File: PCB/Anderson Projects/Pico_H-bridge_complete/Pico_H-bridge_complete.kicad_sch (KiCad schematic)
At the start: 40 parts, among them J1 Screw_Terminal_01x10, J2 Motor Connector, SW1 SW_DIP_x01, U1 Pico, U2 ILD217T, U3 ILD217T, U4 ILD217T, U5 OPA4197

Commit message: Anderson Schematic with opto-couples prior to change to zener diodes
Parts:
- added C20: 0.1uF, Capacitor_SMD:C_0805_2012Metric, symbol Device:C
- added C21: 1uF, Capacitor_SMD:C_0805_2012Metric, symbol Device:C
- D3: value 3.6V -> 3.3v
- R10, R4, R6, R8: value 4.7k -> 10k
- R21, R23: value 4.7k -> 1kΩ
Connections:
- net +3.3V: now also U1.35 (ADC_VREF), C20.1, C21.1
- net GND: now also U1.33 (AGND), C20.2, C21.2
- no-connect marks 20 -> 18
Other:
- moved on the sheet: D3, R24, R25, RV1

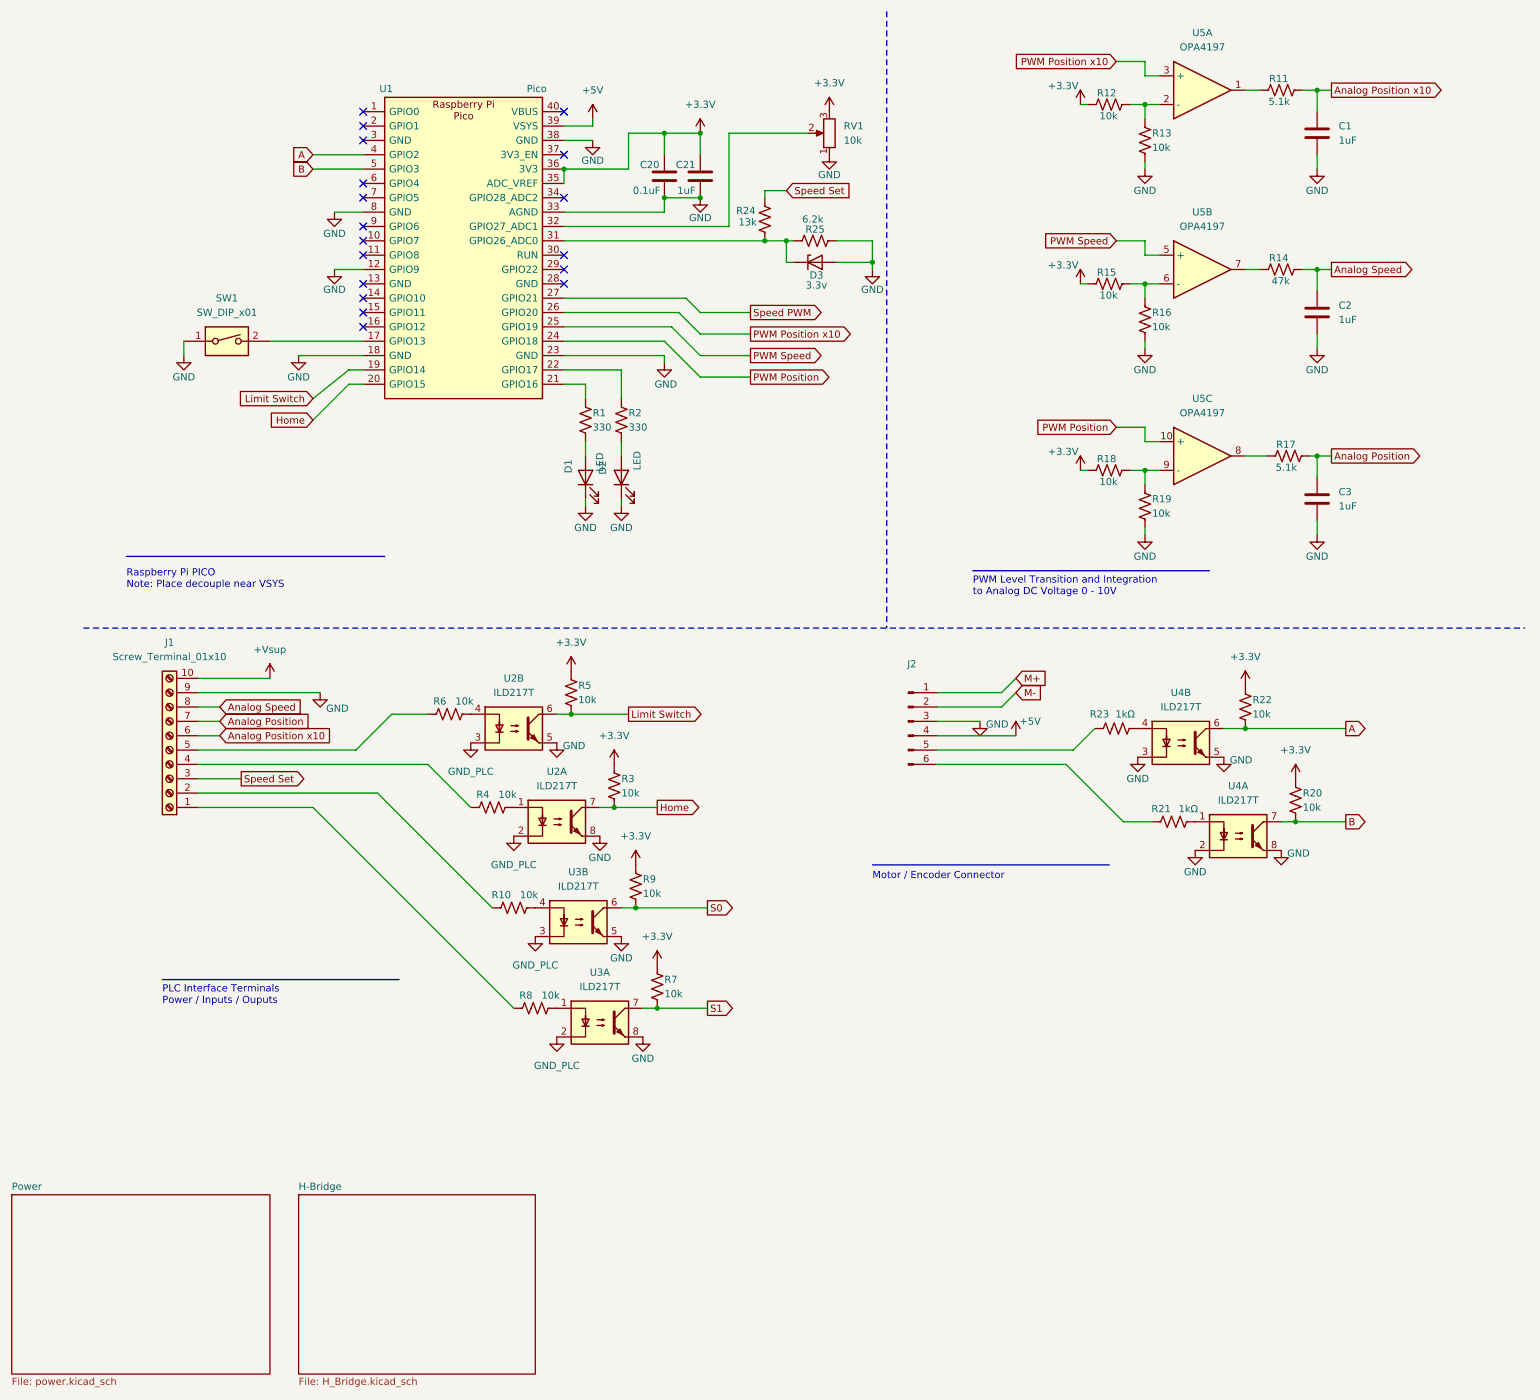
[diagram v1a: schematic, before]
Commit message: Changed Dig inputs  to zener buffers, removed all opto-couples, rebuilt h-bridge logic.
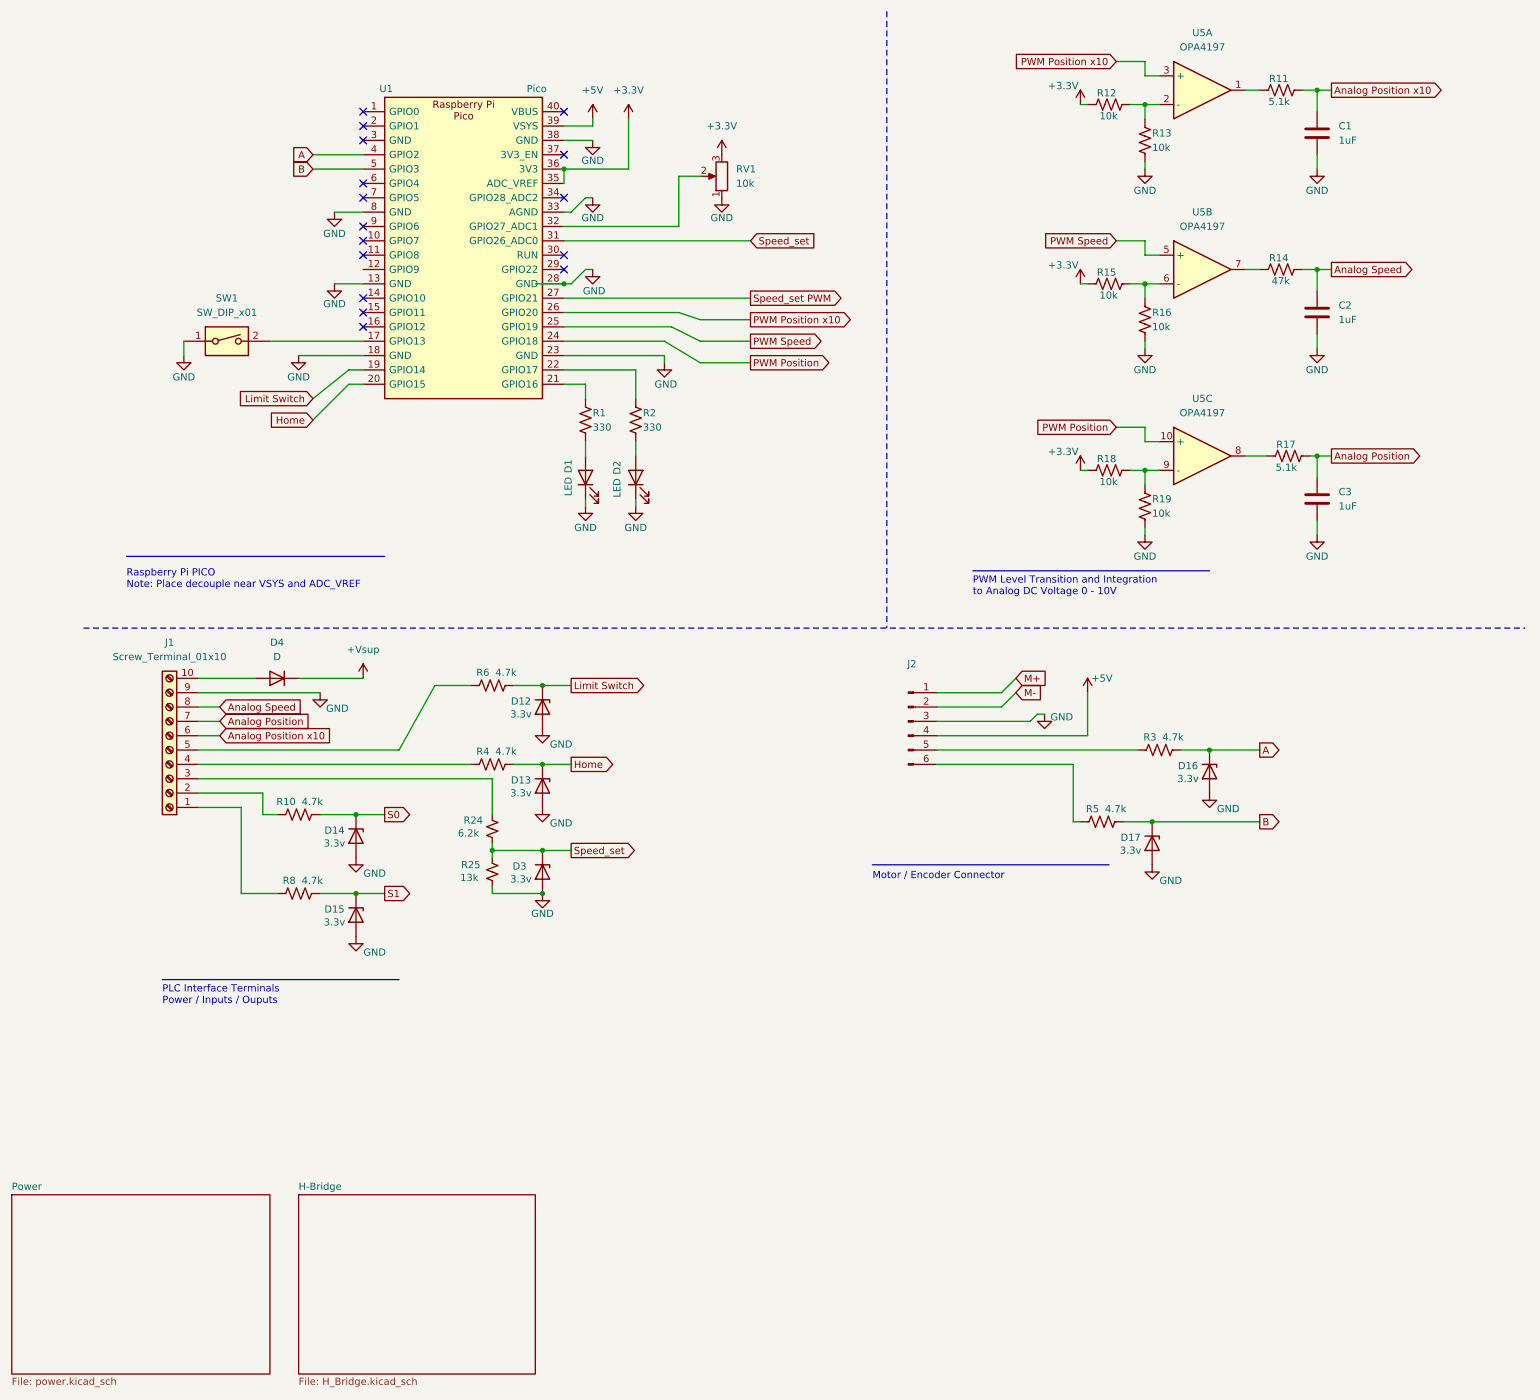
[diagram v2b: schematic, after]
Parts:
- removed C20: 0.1uF, Capacitor_SMD:C_0805_2012Metric, symbol Device:C
- removed C21: 1uF, Capacitor_SMD:C_0805_2012Metric, symbol Device:C
- removed R20, R22, R7, R9: 10k, Resistor_SMD:R_0201_0603Metric, symbol Device:R_US
- removed R21, R23: 1kΩ, Resistor_SMD:R_0201_0603Metric, symbol Device:R_US
- removed U2, U3, U4: ILD217T, CustomBPA:SOIC-8_5.46mm_P1.27, symbol CustomBPA:ILD217T
- added D12, D13, D14, D15, D16, D17: 3.3v, Diode_SMD:D_SOD-323, symbol Diode:Z1SMAxxx
- added D4: D, symbol Device:D
- C1, C2, C3: footprint Capacitor_THT:C_Rect_L7.2mm_W4.5mm_P5.00mm_FKS2_FKP2_MKS2_MKP2 -> Capacitor_SMD:C_1206_3216Metric
- D3: footprint Diode_SMD:D_SOD-123 -> Diode_SMD:D_SOD-323
- R10, R3, R4, R5, R6, R8: value 10k -> 4.7k
- R24, R25: symbol Device:R_US -> Device:R_Small_US
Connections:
- net +3.3V: no longer R3.1, R5.1
- net +Vsup: now also D4.1 (K); no longer J1.10 (Pin_10)
- net A: now also R3.2, D16.1 (K)
- net B: now also R5.2, D17.1 (K)
- net GND: now also R25.2, U1.13 (GND), U1.28 (GND), D12.2 (A), D13.2 (A), D14.2 (A), D15.2 (A), D16.2 (A), D17.2 (A); no longer R25.1, U1.12 (GPIO9)
- net Home: now also R4.2, D13.1 (K); no longer R3.2
- net Limit Switch: now also R6.2, D12.1 (K); no longer R5.2
- net S0: now also R10.2, D14.1 (K)
- net S1: now also R8.2, D15.1 (K)
- net Speed_set: now reaches D3.1 (K), R24.2, U1.31 (GPIO26_ADC0)
- net Speed_set: now also R25.1; no longer R25.2
- net at J2.5 (Pin_5): now also R3.1
- net at J2.6 (Pin_6): now also R5.1
- net Speed PWM renamed Speed_set PWM
- net Speed Set: no longer names the net of J1.3 (Pin_3), R24.1
- new net: D4.2 (A), J1.10 (Pin_10)
- no-connect marks 18 -> 16
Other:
- note added: "Raspberry Pi PICO Note: Place decouple near VSYS and ADC_VREF"
- note removed: "Raspberry Pi PICO Note: Place decouple near VSYS"
- moved on the sheet: D2, D3, R10, R2, R4, R6, R8, RV1

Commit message: Anderson PCB ready for board layout
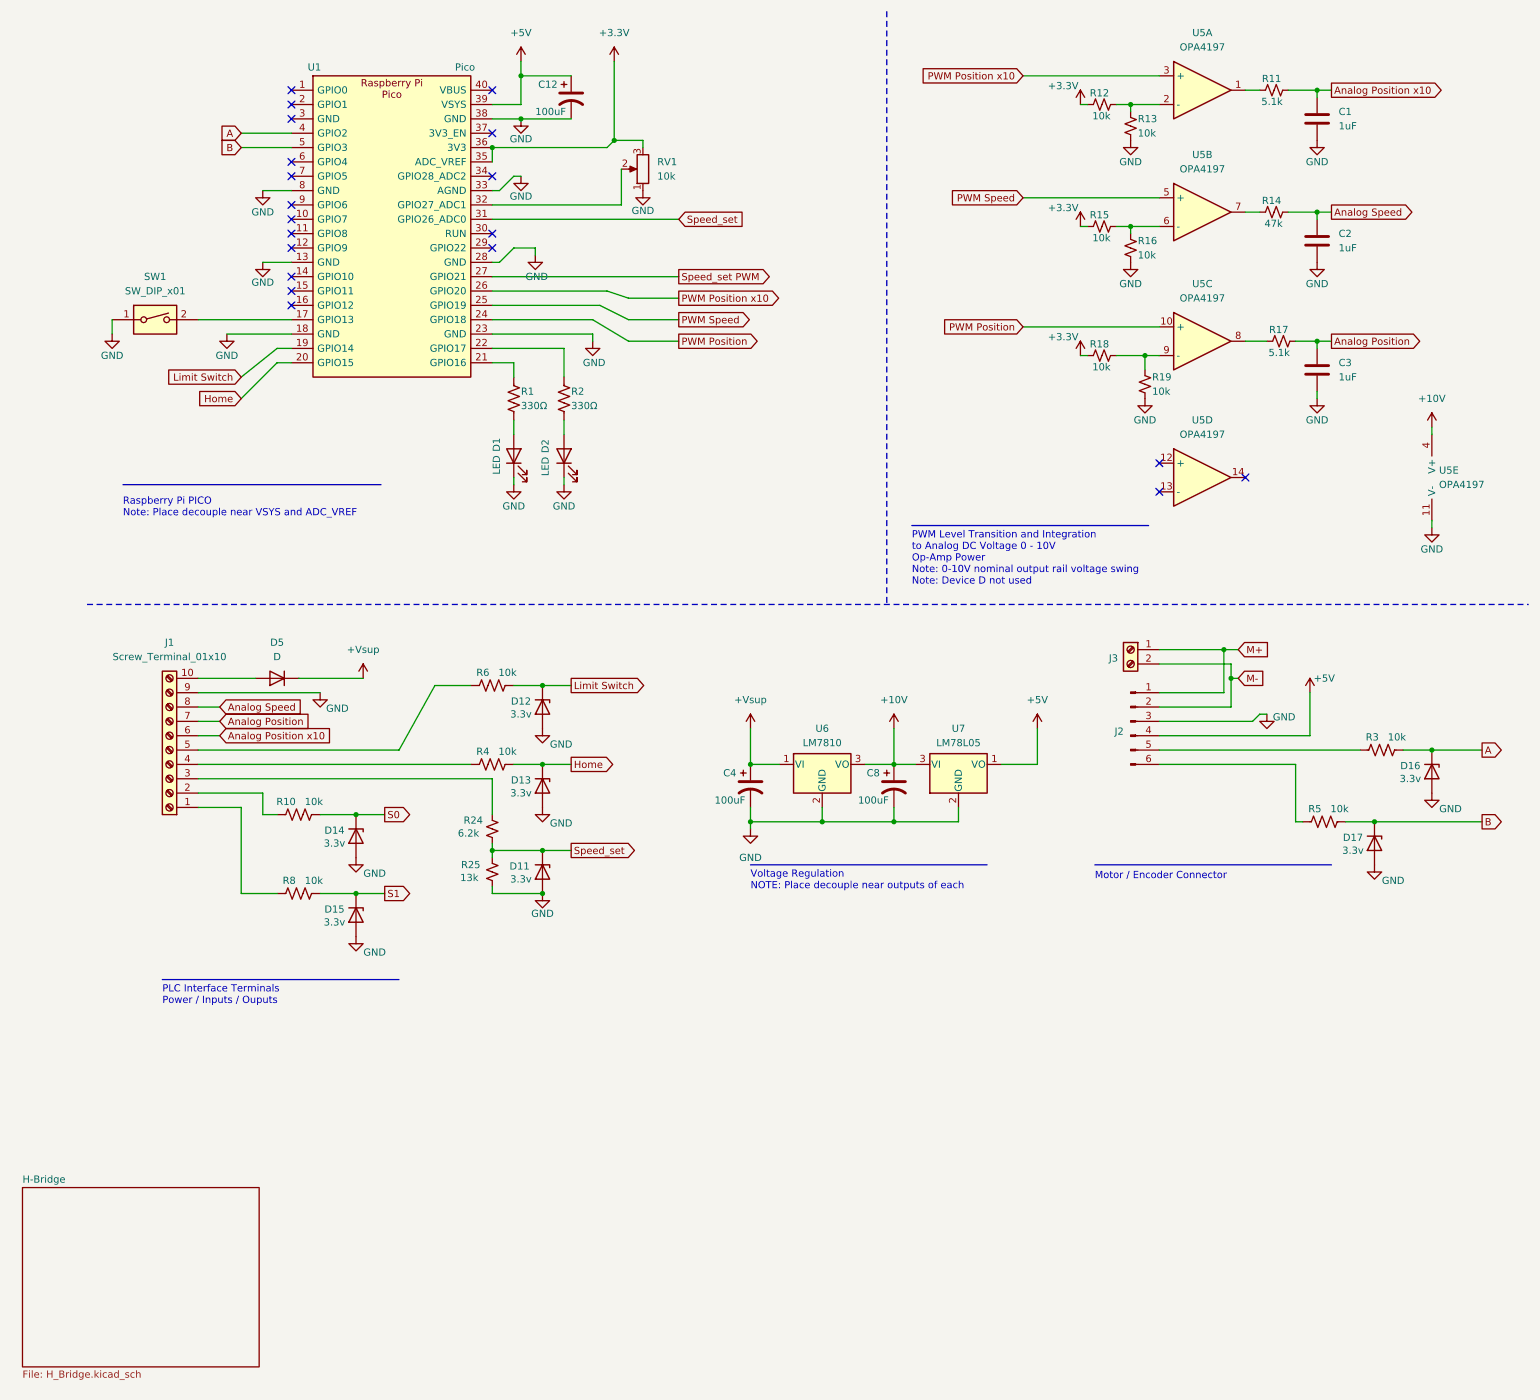
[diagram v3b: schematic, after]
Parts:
- added C12, C4, C8: 100uF, Capacitor_SMD:C_1210_3225Metric, symbol Device:C_Polarized_US
- added J3: Screw_Terminal_01x02, TerminalBlock_Phoenix:TerminalBlock_Phoenix_MKDS-1,5-2_1x02_P5.00mm_Horizontal, symbol Connector:Screw_Terminal_01x02
- added unit 4 of U5
- added unit 5 of U5
- added U6: LM7810, Package_TO_SOT_SMD:SOT-89-3, symbol Regulator_Linear:LM7810_TO220
- added U7: LM78L05, Package_TO_SOT_SMD:SOT-89-3, symbol Regulator_Linear:LM78L05_TO92
- D1, D2: footprint LED_SMD:LED_0805_2012Metric -> LED_SMD:LED_0603_1608Metric
- D5: renamed from D4; footprint (none) -> Diode_SMD:D_SMA
- R1, R2: value 330 -> 330Ω; footprint Resistor_SMD:R_0201_0603Metric -> Resistor_SMD:R_0603_1608Metric
- R10, R3, R4, R5, R6, R8: value 4.7k -> 10k; footprint Resistor_SMD:R_0201_0603Metric -> Resistor_SMD:R_0603_1608Metric
- R11, R12, R13, R14, R15, R16, R17, R18, R19: footprint Resistor_SMD:R_0201_0603Metric -> Resistor_SMD:R_0603_1608Metric; symbol Device:R_US -> Device:R_Small_US
- R24, R25: footprint Resistor_SMD:R_0201_0603Metric -> Resistor_SMD:R_0603_1608Metric
- RV1: footprint Potentiometer_SMD:Potentiometer_ACP_CA6-VSMD_Vertical -> Potentiometer_SMD:Potentiometer_Bourns_3314J_Vertical
- SW1: footprint Button_Switch_SMD:SW_DIP_SPSTx01_Slide_6.7x4.1mm_W8.61mm_P2.54mm_LowProfile -> CustomBPA:DIP_1x01_3.5_6.2mm
- U5: symbol Amplifier_Operational:OPA4197xPW -> CustomBPA:OPA4197xPW
- renumbered D3 to D11
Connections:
- net +5V: now also C12.1, U7.1 (VO)
- net +Vsup: now also C4.1, U6.1 (VI)
- net GND: now also C12.2, C4.2, C8.2, U5.11 (V-), U6.2 (GND), U7.2 (GND)
- net M+: now also J3.1 (Pin_1)
- net M-: now also J3.2 (Pin_2)
- new net +10V: C8.1, U5.4 (V+), U6.3 (VO), U7.3 (VI)
- no-connect marks 16 -> 20
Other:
- removed sheet Power
- note added: "PWM Level Transition and Integration to Analog DC Voltage 0 - 10V Op-Amp Power Note: 0-10V nominal output rail voltage swing Note: Device D not used"
- note added: "Voltage Regulation NOTE: Place decouple near outputs of each"
- note removed: "PWM Level Transition and Integration to Analog DC Voltage 0 - 10V"
- moved on the sheet: C1, C2, C3, D1, D16, D17, D2, J2, R1, R2, R3, R5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

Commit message: Anderson Pico_H-bridge_complete Gerbers ready to order
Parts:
- added TP1: Spd(0-3.3), TestPoint:TestPoint_Plated_Hole_D2.0mm, symbol Connector:TestPoint
- added TP2: 10v, TestPoint:TestPoint_Plated_Hole_D2.0mm, symbol Connector:TestPoint
- added TP3: 5v, TestPoint:TestPoint_Plated_Hole_D2.0mm, symbol Connector:TestPoint
- U1: footprint Module:RaspberryPi_Pico_Common_Unspecified -> CustomBPA:RaspberryPi_Pico
- U6: symbol Regulator_Linear:LM7810_TO220 -> Regulator_Linear:L78L10_SOT89
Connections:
- net +10V: now also U6.1 (OUT), TP2.1; no longer U6.3 (VO)
- net +5V: now also TP3.1
- net +Vsup: now also U6.3 (IN); no longer U6.1 (VI)
- net M+: now also J3.2 (Pin_2); no longer J3.1 (Pin_1)
- net M-: now also J3.1 (Pin_1); no longer J3.2 (Pin_2)
- net Speed_set: now also TP1.1

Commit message: minor edits prior to ordering, and assembly document creation
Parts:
- C1, C2, C3: LCSC (none) -> C2167419
- C12, C4, C8: LCSC (none) -> C23742
- D1: value LED -> LED_R; LCSC (none) -> C2286
- D11, D12, D13, D14, D15, D16, D17: LCSC (none) -> C19077437
- D2: value LED -> LED_W; LCSC (none) -> C2290
- D5: LCSC (none) -> C8678
- R1, R2: LCSC (none) -> C23138
- R10, R12, R13, R15, R16, R18, R19, R3, R4, R5, R6, R8: LCSC (none) -> C25804
- R11, R17: LCSC (none) -> C23186
- R14: LCSC (none) -> C25819
- R24: LCSC (none) -> C4260
- R25: LCSC (none) -> C22797
- RV1: value 10k -> 10k pot; LCSC (none) -> C36376
- SW1: LCSC (none) -> C600988
- U5: LCSC (none) -> C2058532
- U6: LCSC (none) -> C122848
- U7: LCSC (none) -> C347258
